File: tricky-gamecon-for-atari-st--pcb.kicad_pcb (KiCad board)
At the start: 2 copper layers, 109.2 x 45.7 mm, 22 parts, among them J1 Conn_01x09, SW1 GrayHill_series_78_SPDT_DIP_x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, SW2 SW_SPST, SW3 SW_SPST, SW4 SW_SPST, SW5 SW_SPST, SW6 SW_SPST, SW7 SW_SPST, SW8 SW_SPST, SW9 SW_SPST

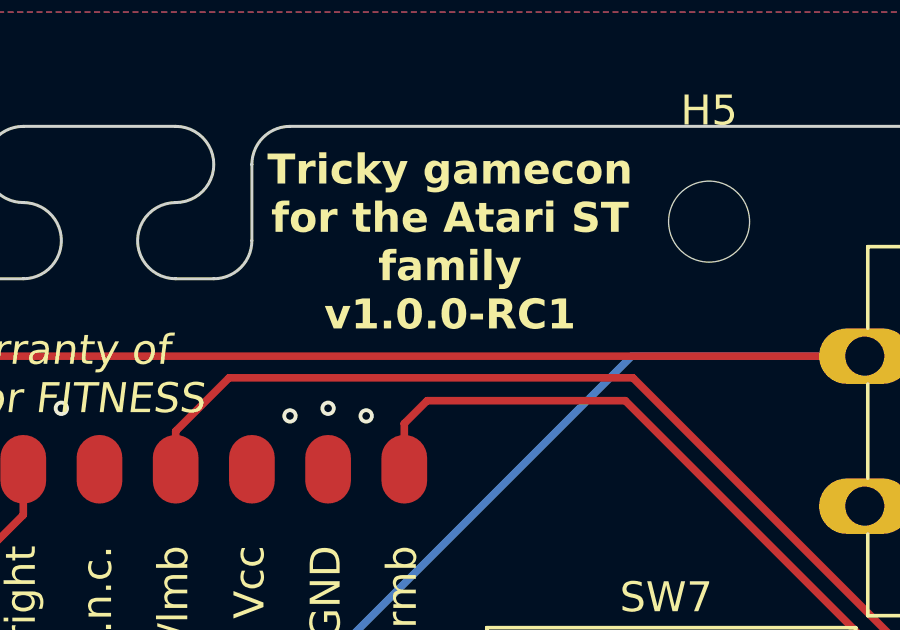
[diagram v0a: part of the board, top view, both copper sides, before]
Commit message: synchronize schematic version, pcb version and pcb silkscreen with git tag
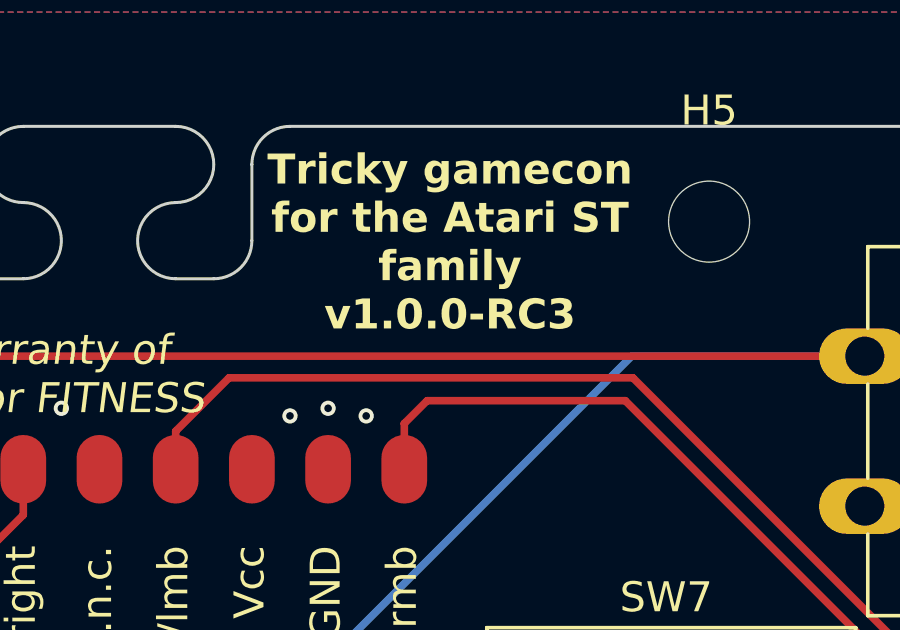
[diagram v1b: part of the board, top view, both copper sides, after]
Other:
- board text added: "Tricky gamecon for the Atari ST family v1.0.0-RC3"
- board text removed: "Tricky gamecon for the Atari ST family v1.0.0-RC1"
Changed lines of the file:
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@@
     (title "Tricky GAMe CONtroller for the Atari ST family -- PCB")
     (date "2023-11-14")
-    (rev "v1.0.0-RC2")
+    (rev "v1.0.0-RC3")
     (company "Sporniket")
     (comment 3 "https://github.com/sporniket/tricky-gamecon-for-atari-st--pcb")
@@
     (effects (font (size 1 1) (thickness 0.15) italic) (justify left bottom))
   )
-  (gr_text "Tricky gamecon\nfor the Atari ST\nfamily\nv1.0.0-RC1" (at 100.584 104.648) (layer "F.SilkS")
+  (gr_text "Tricky gamecon\nfor the Atari ST\nfamily\nv1.0.0-RC3" (at 100.584 104.648) (layer "F.SilkS")
     (effects (font (size 1 1) (thickness 0.2) bold) (justify bottom))
   )
